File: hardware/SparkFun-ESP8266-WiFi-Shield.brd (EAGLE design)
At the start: 59.7 x 53.3 mm, 61 parts, among them Q1 BSS138, Q2 BSS138, U1 AP2112K-3.3V, U2 ESP8266, U3 AT25SF041-SOIC8, Y1 26MHz

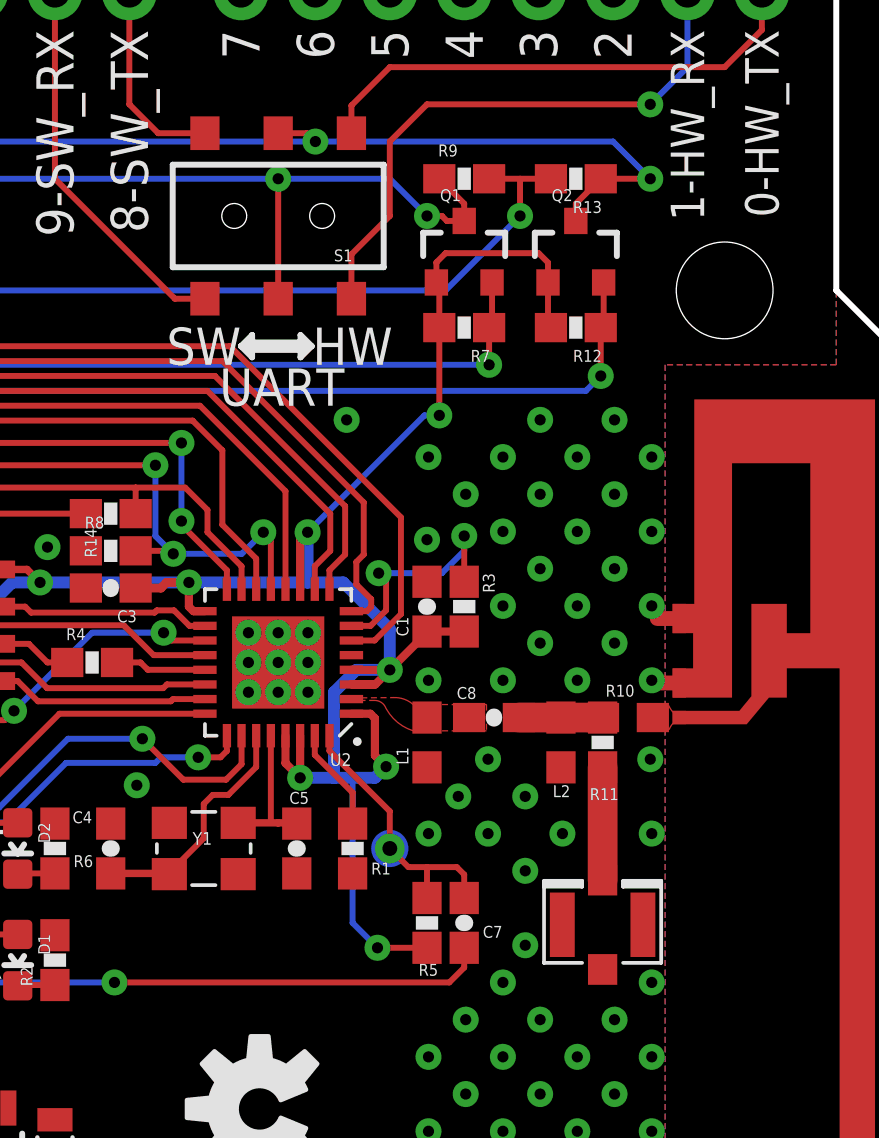
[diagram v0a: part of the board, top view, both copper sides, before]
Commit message: Fixing U.FL name and value, minor re-routing.
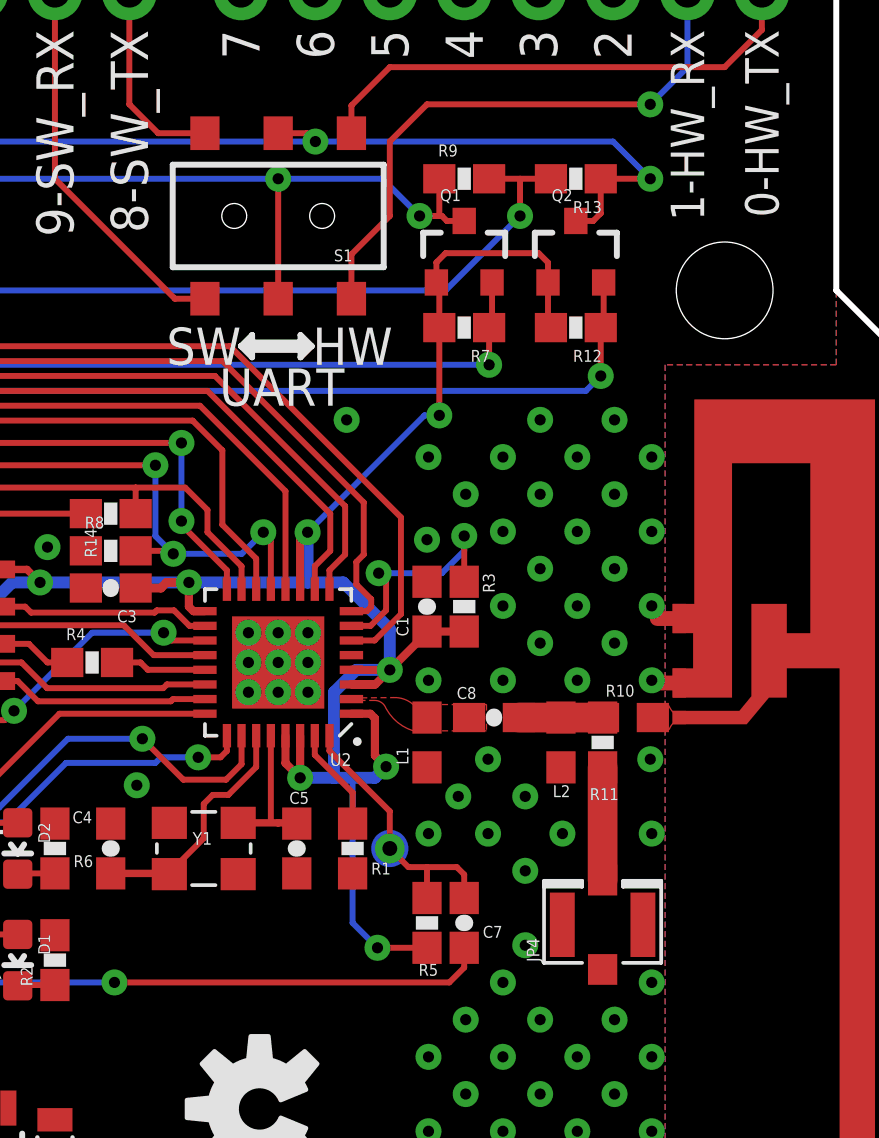
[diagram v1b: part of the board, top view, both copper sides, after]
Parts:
- renumbered E2 to JP4

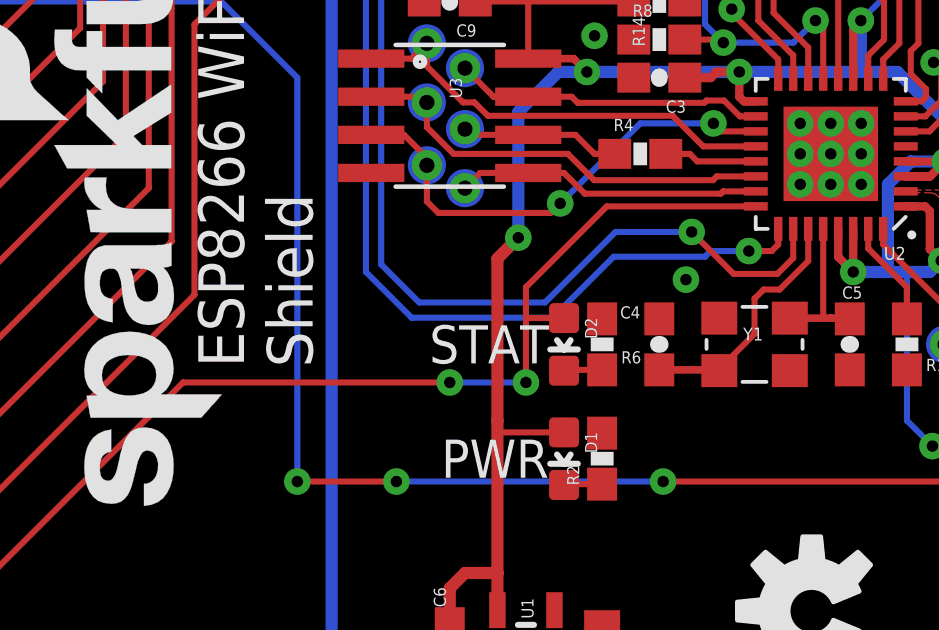
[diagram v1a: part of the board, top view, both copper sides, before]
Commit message: Changing STAT LED to active low.
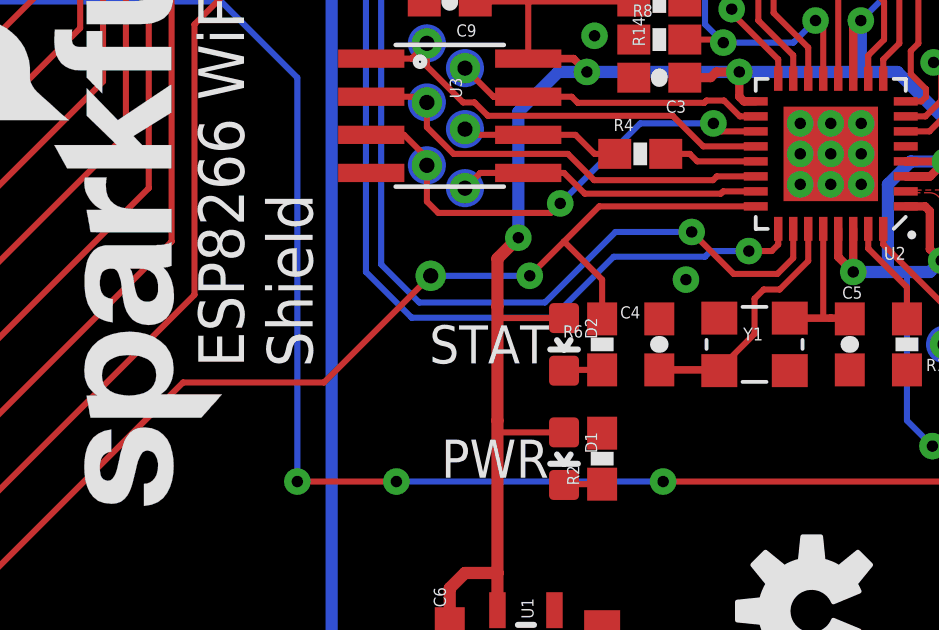
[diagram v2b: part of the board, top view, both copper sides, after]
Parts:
- turned R6 to 270 degrees
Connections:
- removed net N$15: D2.C, R6.1
- new net N$9: D2.C, R6.2
- net GND: no longer R6.2
- net GPIO5: now also R6.1; no longer D2.A
- net VCC: now also D2.A
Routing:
- net VCC: track 102.6 -> 105.2 mm
- net N$15: track 1.30 -> 0.00 mm
- net N$9: track 0.00 -> 1.28 mm

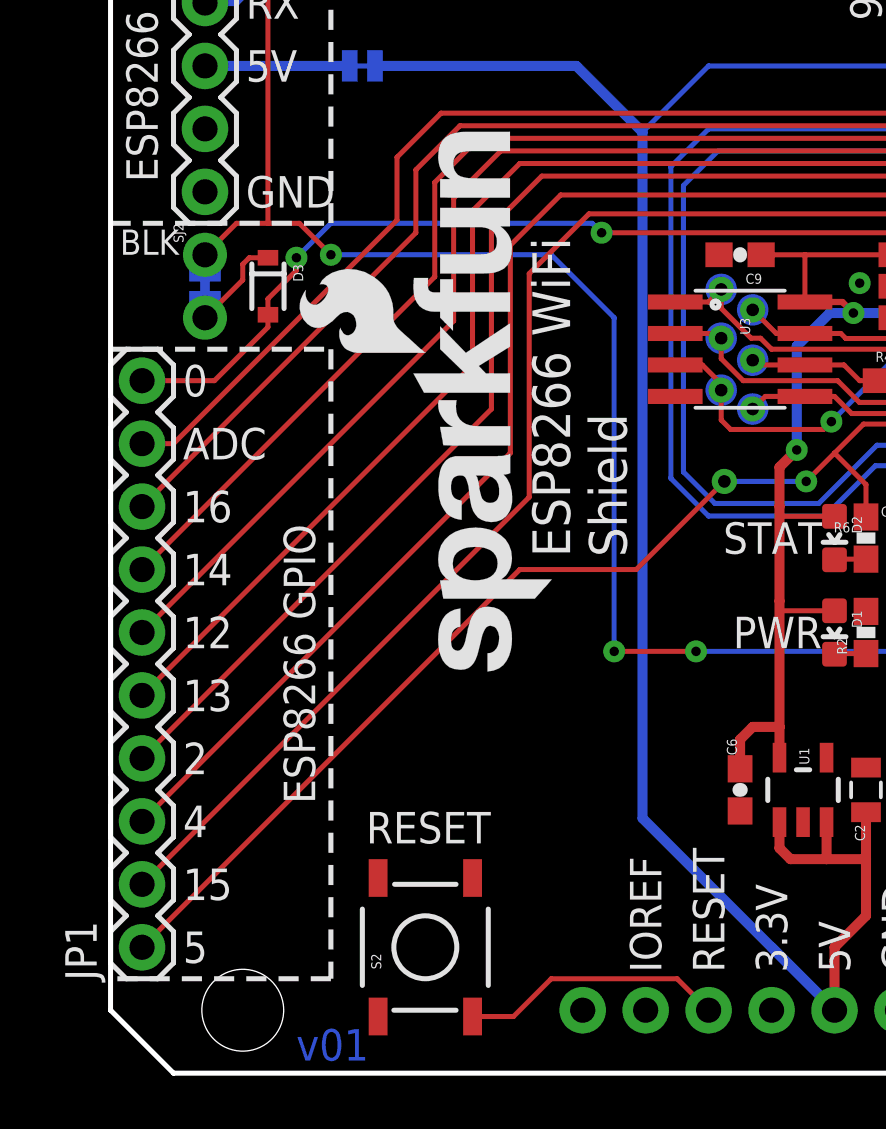
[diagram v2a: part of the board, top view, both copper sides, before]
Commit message: Connecting GPIO4 to Arduino RST.
Upping version to v10.
Should allow for remote bootloading.
Jumper in-line to disconnect if necessary.
Defaulting DTR jumpers to open.
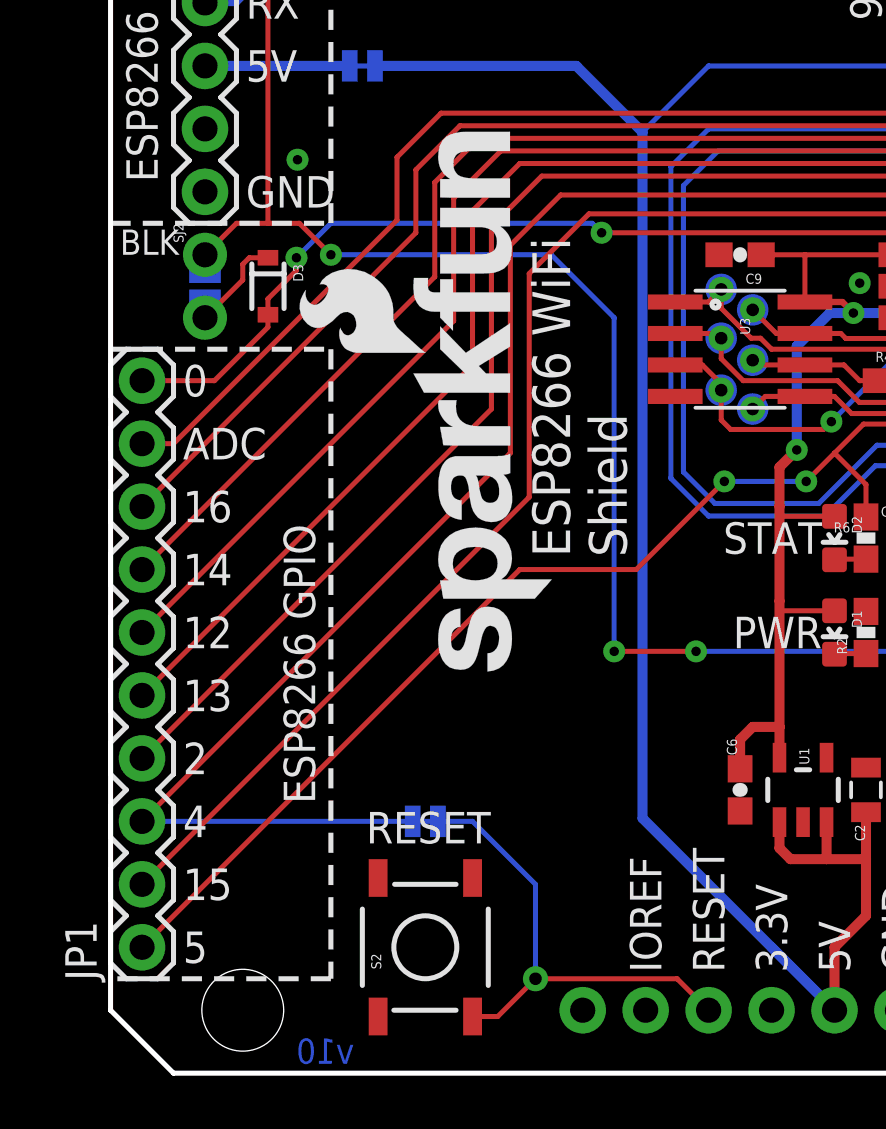
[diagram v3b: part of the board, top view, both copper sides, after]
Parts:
- added SJ4: (no value), SparkFun-Passives:PAD-JUMPER-2-NC_BY_TRACE_YES_SILK
- SJ1: device SparkFun-Passives:PAD-JUMPER-2-NC_BY_TRACE_YES_SILK -> SparkFun-Passives:PAD-JUMPER-2-NO_NO_SILK
- SJ2: device SparkFun-Passives:PTH-JUMPER-NC_BOTTOM_NO_SILK -> SparkFun-Passives:PTH-JUMPER-2-NO_NO_SILK
- turned SJ1 to 270 degrees
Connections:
- removed net N$8: JP3.RES, S2.3
- new net ARD_RST: JP3.RES, S2.3, SJ4.1
- net DTR: now also SJ1.1; no longer SJ1.2
- net GPIO4: now also SJ4.2
- net SJ2: now also SJ1.2; no longer SJ1.1
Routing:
- net ARD_RST: track 0.00 -> 19.5 mm, vias 0 -> 1
- net GPIO4: track 54.5 -> 65.5 mm
- net N$8: track 10.7 -> 0.00 mm
- net GND: vias 72 -> 73
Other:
- board text added: "ARD-RST EN"
- board text added: "RST"
- board text added: "v10"
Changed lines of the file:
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@@
 <layer number="56" name="wert" color="7" fill="1" visible="no" active="no"/>
 <layer number="57" name="tCAD" color="7" fill="1" visible="no" active="no"/>
+<layer number="59" name="tCarbon" color="7" fill="1" visible="no" active="no"/>
+<layer number="60" name="bCarbon" color="7" fill="1" visible="no" active="no"/>
 <layer number="90" name="Modules" color="5" fill="1" visible="no" active="no"/>
 <layer number="91" name="Nets" color="2" fill="1" visible="no" active="no"/>
@@
 <layer number="127" name="_tValues" color="7" fill="1" visible="no" active="yes"/>
 <layer number="128" name="_bValues" color="7" fill="1" visible="no" active="yes"/>
+<layer number="129" name="Mask" color="7" fill="1" visible="yes" active="yes"/>
 <layer number="131" name="tAdjust" color="7" fill="1" visible="no" active="yes"/>
 <layer number="132" name="bAdjust" color="7" fill="1" visible="no" active="yes"/>
@@
 <layer number="223" name="223bmp" color="24" fill="1" visible="no" active="no"/>
 <layer number="224" name="224bmp" color="25" fill="1" visible="no" active="no"/>
+<layer number="225" name="225bmp" color="7" fill="1" visible="yes" active="yes"/>
+<layer number="226" name="226bmp" color="7" fill="1" visible="yes" active="yes"/>
+<layer number="227" name="227bmp" color="7" fill="1" visible="yes" active="yes"/>
+<layer number="228" name="228bmp" color="7" fill="1" visible="yes" active="yes"/>
+<layer number="229" name="229bmp" color="7" fill="1" visible="yes" active="yes"/>
+<layer number="230" name="230bmp" color="7" fill="1" visible="yes" active="yes"/>
+<layer number="231" name="231bmp" color="7" fill="1" visible="yes" active="yes"/>
 <layer number="248" name="Housing" color="7" fill="1" visible="no" active="yes"/>
 <layer number="249" name="Edge" color="7" fill="1" visible="no" active="yes"/>
@@
 <text x="28.702" y="20.828" size="1.524" layer="22" font="vector" ratio="15" rot="MR0" align="top-left">ESP8266 WiFi
 Shield</text>
+<text x="12.7" y="11.43" size="0.889" layer="22" font="vector" ratio="15" rot="MR0" align="bottom-center">ARD-RST
+EN</text>
+<text x="11.43" y="10.16" size="0.889" layer="22" font="vector" ratio="15" rot="MR0" align="center-left">4</text>
+<text x="13.716" y="10.16" size="0.889" layer="22" font="vector" ratio="15" rot="MR0" align="center-right">RST</text>
+<text x="7.493" y="0.889" size="1.016" layer="16" font="vector" ratio="15" rot="MR0" align="center-right">v10</text>
 </plain>
 <attributes>
@@
 </element>
 <element name="FRAME1" library="SparkFun-Aesthetics" package="CREATIVE_COMMONS" value="" x="-2.032" y="-23.622" smashed="yes">
-<attribute name="VERSION" value="v01" x="7.493" y="0.508" size="1.27" layer="16" font="vector" ratio="15"/>
+<attribute name="VERSION" value="v01" x="7.493" y="0.508" size="1.27" layer="16" font="vector" ratio="15" display="off"/>
 <attribute name="DESIGNER" value="Jim Lindblom" x="28.448" y="-23.622" size="1.778" layer="51"/>
 </element>
@@
 <attribute name="PROD_ID" value="DIO-09646" x="6.35" y="31.75" size="1.778" layer="27" font="vector" ratio="15" rot="R270" display="off"/>
 </element>
-<element name="SJ2" library="SparkFun-Passives" package="PTH-JUMPER-NC_BOTTOM_NO_SILK" value="" x="3.81" y="31.75" rot="R270"/>
 <element name="D1" library="SparkFun-LED" package="LED-0603" value="RED" x="29.21" y="17.78" rot="R180">
 <attribute name="PROD_ID" value="DIO-00819" x="29.21" y="17.78" size="0.8128" layer="27" font="vector" ratio="15" rot="R180" display="off"/>
 </element>
-<element name="SJ1" library="SparkFun-Passives" package="PAD-JUMPER-2-NC_BY_TRACE_YES_SILK" value="" x="3.81" y="31.75" rot="MR90"/>
 <element name="JP3" library="SparkFun-Boards" package="UNO_R3_SHIELD_NOLABELS" value="ARDUINO_R3_SHIELDNOLABELS" x="0" y="53.34" rot="R270"/>
 <element name="Q1" library="SparkFun-DiscreteSemi" package="SOT23-3" value="BSS138" x="44.45" y="41.91">
@@
 <attribute name="PROD_ID" value="CONN-09193" x="49.1744" y="18.9865" size="0.889" layer="27" font="vector" ratio="15" rot="R90" display="off"/>
 </element>
+<element name="SJ4" library="SparkFun-Passives" package="PAD-JUMPER-2-NC_BY_TRACE_YES_SILK" value="" x="12.7" y="10.16" rot="MR0"/>
+<element name="SJ1" library="SparkFun-Passives" package="PAD-JUMPER-2-NO_NO_SILK" value="" x="3.81" y="31.75" rot="MR270"/>
+<element name="SJ2" library="SparkFun-Passives" package="PTH-JUMPER-2-NO_NO_SILK" value="" x="3.81" y="31.75" rot="R270"/>
 </elements>
 <signals>
@@
 <contactref element="JP4" pad="P$1"/>
 <contactref element="JP4" pad="P$2"/>
+<via x="7.5438" y="36.8554" extent="1-16" drill="0.381"/>
 </signal>
 <signal name="N$1">
@@
 <signal name="DTR">
 <contactref element="C7" pad="2"/>
-<contactref element="SJ2" pad="1"/>
-<contactref element="SJ1" pad="2"/>
-<wire x1="3.81" y1="32.258" x2="3.81" y2="33.02" width="0.2032" layer="16"/>
 <contactref element="JP2" pad="DTR"/>
 <wire x1="44.45" y1="18.2" x2="44.45" y2="17.526" width="0.2032" layer="1"/>
@@
 <wire x1="6.35" y1="34.29" x2="7.62" y2="34.29" width="0.2032" layer="1"/>
 <wire x1="7.62" y1="34.29" x2="8.89" y2="33.02" width="0.2032" layer="1"/>
+<contactref element="SJ1" pad="1"/>
+<contactref element="SJ2" pad="1"/>
+<wire x1="3.81" y1="32.2" x2="3.81" y2="33.02" width="0.2032" layer="16"/>
 </signal>
 <signal name="GPIO14/SCL">
@@
 <wire x1="29.21" y1="25.019" x2="28.067" y2="23.876" width="0.2032" layer="1"/>
 <wire x1="28.067" y1="23.876" x2="24.765" y2="23.876" width="0.2032" layer="16"/>
-<via x="24.765" y="23.876" extent="1-16" drill="0.508"/>
+<via x="24.765" y="23.876" extent="1-16" drill="0.381"/>
 <wire x1="24.765" y1="23.876" x2="21.209" y2="20.32" width="0.2032" layer="1"/>
 <wire x1="30.48" y1="22.44" x2="30.48" y2="23.749" width="0.2032" layer="1"/>
@@
 <wire x1="16.129" y1="25.019" x2="16.129" y2="33.401" width="0.2032" layer="1"/>
 <wire x1="16.129" y1="33.401" x2="18.161" y2="35.433" width="0.2032" layer="1"/>
+<contactref element="SJ4" pad="2"/>
+<wire x1="1.27" y1="10.16" x2="12.192" y2="10.16" width="0.2032" layer="16"/>
 </signal>
 <signal name="SD_!WP!">
@@
 <signal name="SJ2">
 <contactref element="D3" pad="C"/>
-<contactref element="SJ2" pad="2"/>
-<contactref element="SJ1" pad="1"/>
-<wire x1="3.81" y1="31.242" x2="3.81" y2="30.48" width="0.2032" layer="16"/>
 <wire x1="6.35" y1="32.9" x2="5.595" y2="32.9" width="0.2032" layer="1"/>
 <wire x1="5.595" y1="32.9" x2="5.334" y2="32.639" width="0.2032" layer="1"/>
 <wire x1="5.334" y1="32.639" x2="5.334" y2="32.004" width="0.2032" layer="1"/>
 <wire x1="5.334" y1="32.004" x2="3.81" y2="30.48" width="0.2032" layer="1"/>
+<contactref element="SJ1" pad="2"/>
+<contactref element="SJ2" pad="2"/>
+<wire x1="3.81" y1="30.48" x2="3.81" y2="31.3" width="0.2032" layer="16"/>
 </signal>
 <signal name="TX_HIGH">
@@
 <wire x1="43.6" y1="43.18" x2="42.926" y2="43.18" width="0.2032" layer="1"/>
 </signal>
-<signal name="N$8">
+<signal name="ARD_RST">
 <contactref element="JP3" pad="RES"/>
 <contactref element="S2" pad="3"/>
-<wire x1="14.605" y1="2.286" x2="16.256" y2="2.286" width="0.2032" layer="1"/>
-<wire x1="16.256" y1="2.286" x2="17.78" y2="3.81" width="0.2032" layer="1"/>
-<wire x1="17.78" y1="3.81" x2="22.86" y2="3.81" width="0.2032" layer="1"/>
+<wire x1="14.605" y1="2.286" x2="15.621" y2="2.286" width="0.2032" layer="1"/>
+<wire x1="15.621" y1="2.286" x2="17.145" y2="3.81" width="0.2032" layer="1"/>
+<wire x1="17.145" y1="3.81" x2="22.86" y2="3.81" width="0.2032" layer="1"/>
 <wire x1="22.86" y1="3.81" x2="24.13" y2="2.54" width="0.2032" layer="1"/>
+<contactref element="SJ4" pad="1"/>
+<wire x1="13.208" y1="10.16" x2="14.605" y2="10.16" width="0.2032" layer="16"/>
+<via x="17.145" y="3.81" extent="1-16" drill="0.508"/>
+<wire x1="17.145" y1="3.81" x2="17.145" y2="7.62" width="0.2032" layer="16"/>
+<wire x1="17.145" y1="7.62" x2="14.605" y2="10.16" width="0.2032" layer="16"/>
 </signal>
 <signal name="ARD_SW_TX">
